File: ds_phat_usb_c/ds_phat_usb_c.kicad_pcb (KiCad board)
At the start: 2 copper layers, 12.3 x 7.9 mm, 4 parts, among them U1 usb_c_6pin, U2 battery_custom, U3 ds_charger_posts

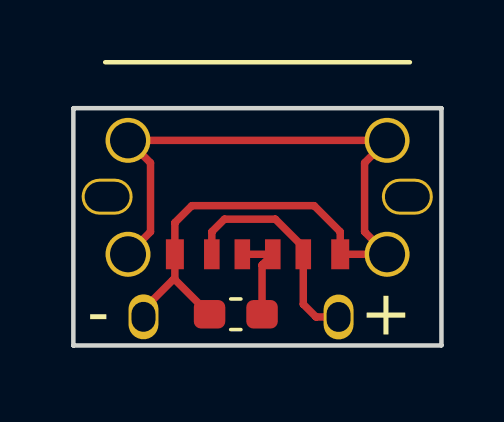
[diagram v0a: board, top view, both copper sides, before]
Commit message: Fixed the design
Now it should be able to be used with any USB C charger
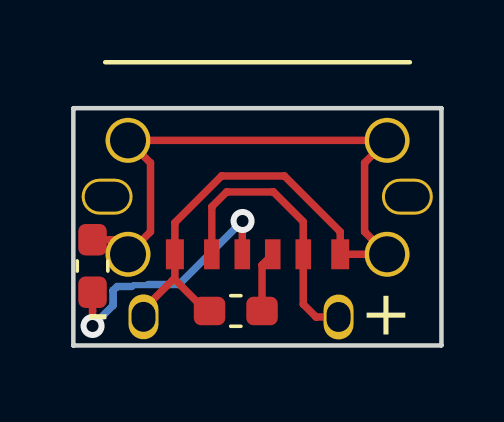
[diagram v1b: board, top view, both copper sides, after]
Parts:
- added R1: R, Resistor_SMD:R_0603_1608Metric_Pad1.05x0.95mm_HandSolder, F.Cu at (143.0, 74.5)
- moved R2 0.11 mm to (147.8, 76.0)
- renumbered R1 to R2
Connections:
- R2 pad 1: Net-(R1-Pad1) -> Net-(U1-CC1)
- U1 pad 3: Net-(R1-Pad1) -> Net-(U1-CC2)
- U1 pad 4: Net-(R1-Pad1) -> Net-(U1-CC1)
- U3 pad 1: Net-(U3-Pad1) -> unconnected-(U3-left-Pad1)
- U3 pad 2: Net-(U3-Pad2) -> unconnected-(U3-right-Pad2)
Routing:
- net Net-(U1-CC2): track 0.00 -> 8.97 mm, vias 0 -> 2
- net Net-(R1-Pad1): track 3.16 -> 0.00 mm
- net Net-(U1-GND): track 31.1 -> 33.3 mm
- net Net-(U1-CC1): track 0.00 -> 2.15 mm
- net Net-(U1-VBUS): track 7.61 -> 9.35 mm
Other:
- net class Default removed
